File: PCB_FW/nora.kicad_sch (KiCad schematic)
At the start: 274 parts, among them J1 USB_C_Receptacle_USB2.0, J2 Conn_01x04, J3 Conn_01x02, J4 Conn_01x02, J5 Conn_02x03_Odd_Even, U1 ATmega32U4-MU, U2 24LC64, U4 Pico, Y1 16MHz

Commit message: WIP 配線中
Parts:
- RE_42: footprint locallib:RotaryEncoder_Alps_EC11K-Switch_Vertical_H20mm -> Rotary_Encoder:RotaryEncoder_Alps_EC11E-Switch_Vertical_H20mm
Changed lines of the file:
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@@
     (property "Reference" "RE_42" (id 0) (at 105.41 266.5435 0))
     (property "Value" "RotaryEncoder_Switch" (id 1) (at 105.41 269.3186 0))
-    (property "Footprint" "locallib:RotaryEncoder_Alps_EC11K-Switch_Vertical_H20mm" (id 2) (at 101.6 271.526 0)
+    (property "Footprint" "Rotary_Encoder:RotaryEncoder_Alps_EC11E-Switch_Vertical_H20mm" (id 2) (at 101.6 271.526 0)
       (effects (font (size 1.27 1.27)) hide)
     )
@@
     )
     (path "/c31541b0-05b3-4f9a-a5ca-240448e17a33"
-      (reference "RE_42") (unit 1) (value "RotaryEncoder_Switch") (footprint "locallib:RotaryEncoder_Alps_EC11K-Switch_Vertical_H20mm")
+      (reference "RE_42") (unit 1) (value "RotaryEncoder_Switch") (footprint "Rotary_Encoder:RotaryEncoder_Alps_EC11E-Switch_Vertical_H20mm")
     )
     (path "/00000000-0000-0000-0000-00005b323aa5"

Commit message: ソケットのシルクに塗りを追加
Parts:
- SW_35, SW_38, SW_40, SW_41, SW_42, SW_43: footprint Keebio-Parts:Kailh-PG1350-1u-MBK-WithKeyName-Socket-1.8mm-hole-reflection -> Keebio-Parts:Kailh-PG1350-1u-MBK-WithKeyName-Socket-1.8mm-hole-reflection-frame-only
- SW_44: footprint Keebio-Parts:Kailh-PG1350-1.5u-MBK-WithKeyName-Socket-1.8mm-hole-reflection -> Keebio-Parts:Kailh-PG1350-1.5u-MBK-WithKeyName-Socket-1.8mm-hole-reflection-frame-only
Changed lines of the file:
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@@
     (property "Reference" "SW_43" (id 0) (at 161.925 95.631 0))
     (property "Value" "R4R" (id 1) (at 161.925 97.9424 0))
-    (property "Footprint" "Keebio-Parts:Kailh-PG1350-1u-MBK-WithKeyName-Socket-1.8mm-hole-reflection" (id 2) (at 161.925 97.79 0)
+    (property "Footprint" "Keebio-Parts:Kailh-PG1350-1u-MBK-WithKeyName-Socket-1.8mm-hole-reflection-frame-only" (id 2) (at 161.925 97.79 0)
       (effects (font (size 1.27 1.27)) hide)
     )
@@
     (property "Reference" "SW_40" (id 0) (at 161.925 30.861 0))
     (property "Value" "R1R" (id 1) (at 161.925 33.1724 0))
-    (property "Footprint" "Keebio-Parts:Kailh-PG1350-1u-MBK-WithKeyName-Socket-1.8mm-hole-reflection" (id 2) (at 161.925 33.02 0)
+    (property "Footprint" "Keebio-Parts:Kailh-PG1350-1u-MBK-WithKeyName-Socket-1.8mm-hole-reflection-frame-only" (id 2) (at 161.925 33.02 0)
       (effects (font (size 1.27 1.27)) hide)
     )
@@
     (property "Reference" "SW_42" (id 0) (at 161.925 74.041 0))
     (property "Value" "R3C" (id 1) (at 161.925 76.3524 0))
-    (property "Footprint" "Keebio-Parts:Kailh-PG1350-1u-MBK-WithKeyName-Socket-1.8mm-hole-reflection" (id 2) (at 161.925 76.2 0)
+    (property "Footprint" "Keebio-Parts:Kailh-PG1350-1u-MBK-WithKeyName-Socket-1.8mm-hole-reflection-frame-only" (id 2) (at 161.925 76.2 0)
       (effects (font (size 1.27 1.27)) hide)
     )
@@
     (property "Reference" "SW_44" (id 0) (at 161.925 114.681 0))
     (property "Value" "Center 1.5u" (id 1) (at 161.925 116.9924 0))
-    (property "Footprint" "Keebio-Parts:Kailh-PG1350-1.5u-MBK-WithKeyName-Socket-1.8mm-hole-reflection" (id 2) (at 161.925 116.84 0)
+    (property "Footprint" "Keebio-Parts:Kailh-PG1350-1.5u-MBK-WithKeyName-Socket-1.8mm-hole-reflection-frame-only" (id 2) (at 161.925 116.84 0)
       (effects (font (size 1.27 1.27)) hide)
     )
@@
     (property "Reference" "SW_38" (id 0) (at 145.415 95.631 0))
     (property "Value" "R4L" (id 1) (at 145.415 97.9424 0))
-    (property "Footprint" "Keebio-Parts:Kailh-PG1350-1u-MBK-WithKeyName-Socket-1.8mm-hole-reflection" (id 2) (at 145.415 97.79 0)
+    (property "Footprint" "Keebio-Parts:Kailh-PG1350-1u-MBK-WithKeyName-Socket-1.8mm-hole-reflection-frame-only" (id 2) (at 145.415 97.79 0)
       (effects (font (size 1.27 1.27)) hide)
     )
@@
     (property "Reference" "SW_41" (id 0) (at 161.925 52.451 0))
     (property "Value" "R2C" (id 1) (at 161.925 54.7624 0))
-    (property "Footprint" "Keebio-Parts:Kailh-PG1350-1u-MBK-WithKeyName-Socket-1.8mm-hole-reflection" (id 2) (at 161.925 54.61 0)
+    (property "Footprint" "Keebio-Parts:Kailh-PG1350-1u-MBK-WithKeyName-Socket-1.8mm-hole-reflection-frame-only" (id 2) (at 161.925 54.61 0)
       (effects (font (size 1.27 1.27)) hide)
     )
@@
     (property "Reference" "SW_35" (id 0) (at 145.415 30.861 0))
     (property "Value" "R1L" (id 1) (at 145.415 33.1724 0))
-    (property "Footprint" "Keebio-Parts:Kailh-PG1350-1u-MBK-WithKeyName-Socket-1.8mm-hole-reflection" (id 2) (at 145.415 33.02 0)
+    (property "Footprint" "Keebio-Parts:Kailh-PG1350-1u-MBK-WithKeyName-Socket-1.8mm-hole-reflection-frame-only" (id 2) (at 145.415 33.02 0)
       (effects (font (size 1.27 1.27)) hide)
     )
@@
     )
     (path "/efce3ccf-dccf-4ab2-825c-383d2306383e"
-      (reference "SW_35") (unit 1) (value "R1L") (footprint "Keebio-Parts:Kailh-PG1350-1u-MBK-WithKeyName-Socket-1.8mm-hole-reflection")
+      (reference "SW_35") (unit 1) (value "R1L") (footprint "Keebio-Parts:Kailh-PG1350-1u-MBK-WithKeyName-Socket-1.8mm-hole-reflection-frame-only")
     )
     (path "/00000000-0000-0000-0000-000061ce9654"
@@
     )
     (path "/cc1d72d3-c085-42d5-b51a-f25583124fcb"
-      (reference "SW_38") (unit 1) (value "R4L") (footprint "Keebio-Parts:Kailh-PG1350-1u-MBK-WithKeyName-Socket-1.8mm-hole-reflection")
+      (reference "SW_38") (unit 1) (value "R4L") (footprint "Keebio-Parts:Kailh-PG1350-1u-MBK-WithKeyName-Socket-1.8mm-hole-reflection-frame-only")
     )
     (path "/00000000-0000-0000-0000-000061ce969c"
@@
     )
     (path "/164abd3f-e22c-4c79-a335-ba856dad611c"
-      (reference "SW_40") (unit 1) (value "R1R") (footprint "Keebio-Parts:Kailh-PG1350-1u-MBK-WithKeyName-Socket-1.8mm-hole-reflection")
+      (reference "SW_40") (unit 1) (value "R1R") (footprint "Keebio-Parts:Kailh-PG1350-1u-MBK-WithKeyName-Socket-1.8mm-hole-reflection-frame-only")
     )
     (path "/ef3363f5-8d79-4ecf-984c-7cb0bf9cde9e"
-      (reference "SW_41") (unit 1) (value "R2C") (footprint "Keebio-Parts:Kailh-PG1350-1u-MBK-WithKeyName-Socket-1.8mm-hole-reflection")
+      (reference "SW_41") (unit 1) (value "R2C") (footprint "Keebio-Parts:Kailh-PG1350-1u-MBK-WithKeyName-Socket-1.8mm-hole-reflection-frame-only")
     )
     (path "/8f0205a6-0769-462f-bc35-3f1d10f4a746"
-      (reference "SW_42") (unit 1) (value "R3C") (footprint "Keebio-Parts:Kailh-PG1350-1u-MBK-WithKeyName-Socket-1.8mm-hole-reflection")
+      (reference "SW_42") (unit 1) (value "R3C") (footprint "Keebio-Parts:Kailh-PG1350-1u-MBK-WithKeyName-Socket-1.8mm-hole-reflection-frame-only")
     )
     (path "/0dea41fa-0c6a-48a7-81ed-660971009e1c"
-      (reference "SW_43") (unit 1) (value "R4R") (footprint "Keebio-Parts:Kailh-PG1350-1u-MBK-WithKeyName-Socket-1.8mm-hole-reflection")
+      (reference "SW_43") (unit 1) (value "R4R") (footprint "Keebio-Parts:Kailh-PG1350-1u-MBK-WithKeyName-Socket-1.8mm-hole-reflection-frame-only")
     )
     (path "/a2f8a0fb-e12c-4d2c-8033-a042712e74d5"
-      (reference "SW_44") (unit 1) (value "Center 1.5u") (footprint "Keebio-Parts:Kailh-PG1350-1.5u-MBK-WithKeyName-Socket-1.8mm-hole-reflection")
+      (reference "SW_44") (unit 1) (value "Center 1.5u") (footprint "Keebio-Parts:Kailh-PG1350-1.5u-MBK-WithKeyName-Socket-1.8mm-hole-reflection-frame-only")
     )
     (path "/00000000-0000-0000-0000-000061d01246"

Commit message: 基板製造ファイル準備
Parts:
- D99: LCSC (none) -> C81598
- R7: LCSC (none) -> C17513
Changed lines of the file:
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@@
+      (effects (font (size 1.27 1.27)) hide)
+    )
+    (property "LCSC" "C81598" (id 4) (at 290.195 179.07 0)
       (effects (font (size 1.27 1.27)) hide)
     )
@@
       (effects (font (size 1.27 1.27)) hide)
     )
+    (property "LCSC" "C17513" (id 4) (at 297.815 176.53 0)
+      (effects (font (size 1.27 1.27)) hide)
+    )

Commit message: パーツ番号変更
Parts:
- C1: LCSC C15850 -> C2922480
- U2: Alternative LCSC (none) -> C6487, C116707, C13645
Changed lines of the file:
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@@
       (effects (font (size 1.27 1.27)) hide)
     )
-    (property "LCSC" "C15850" (id 4) (at 329.565 120.015 0)
+    (property "LCSC" "C2922480" (id 4) (at 329.565 120.015 0)
       (effects (font (size 1.27 1.27)) hide)
     )
@@
       (effects (font (size 1.27 1.27)) hide)
     )
+    (property "Alternative LCSC" "C6487, C116707, C13645" (id 5) (at 386.715 168.91 0)
+      (effects (font (size 1.27 1.27)) hide)
+    )

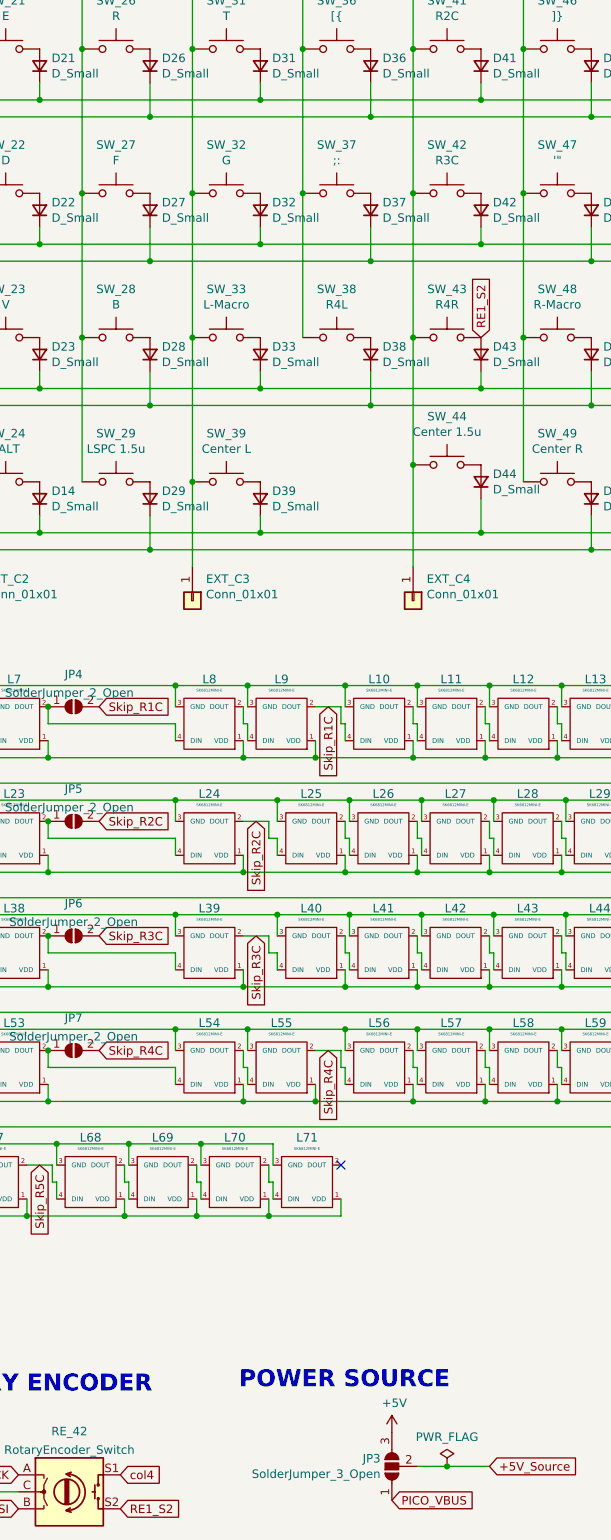
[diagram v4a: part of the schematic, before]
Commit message: ロータリーエンコーダが接続されるマトリクス行を変更
物理的にREが配置される場所に合わせた行へ修正。
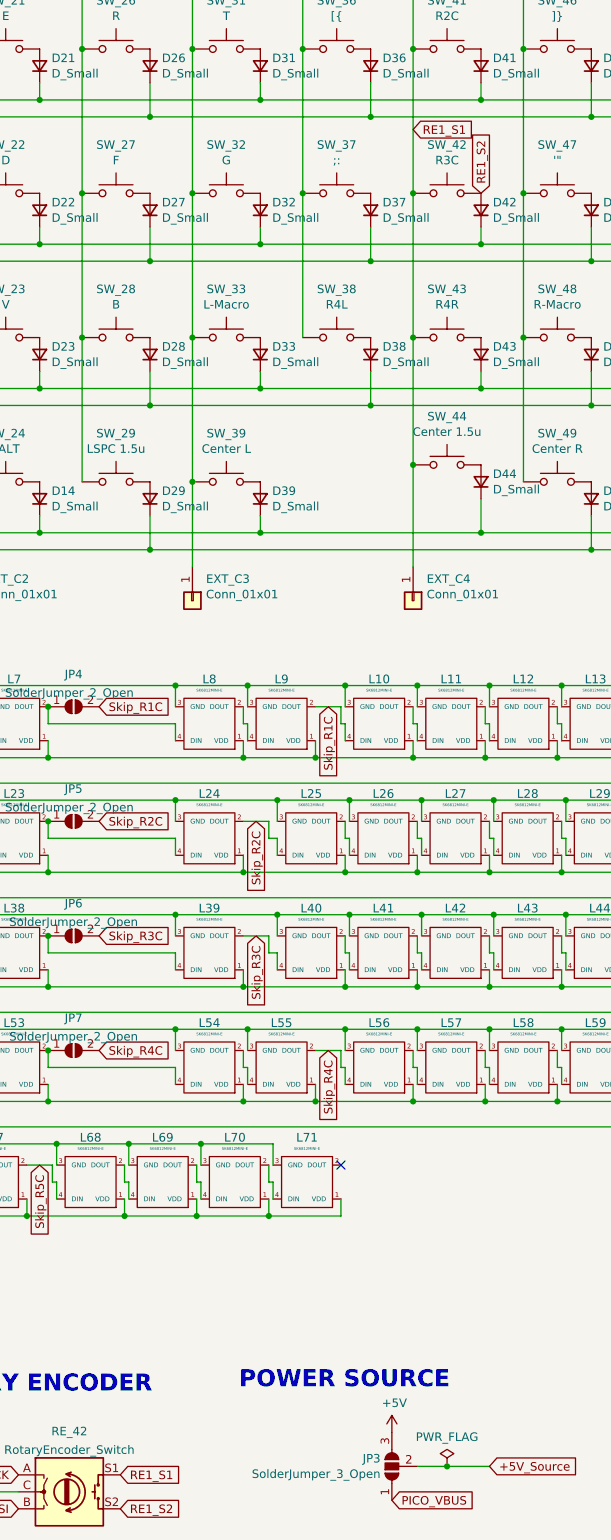
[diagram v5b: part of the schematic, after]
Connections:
- net RE1_S2: now also D42.2 (A), SW_42.2; no longer D43.2 (A), SW_43.2
- net col4 renamed RE1_S1
- new net: D43.2 (A), SW_43.2
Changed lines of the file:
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@@
     )
   )
-  (global_label "col4" (shape input) (at 113.03 273.05 0) (fields_autoplaced)
-    (effects (font (size 1.27 1.27)) (justify left))
-    (property "シート間のリファレンス" "${INTERSHEET_REFS}" (id 0) (at 119.4666 272.9706 0)
+  (global_label "RE1_S1" (shape input) (at 113.03 273.05 0) (fields_autoplaced)
+    (effects (font (size 1.27 1.27)) (justify left))
+    (property "シート間のリファレンス" "${INTERSHEET_REFS}" (id 0) (at 122.3694 272.9706 0)
       (effects (font (size 1.27 1.27)) (justify left) hide)
     )
@@
     )
   )
+  (global_label "RE1_S1" (shape input) (at 156.845 71.755 0) (fields_autoplaced)
+    (effects (font (size 1.27 1.27)) (justify left))
+    (property "シート間のリファレンス" "${INTERSHEET_REFS}" (id 0) (at 166.1844 71.6756 0)
+      (effects (font (size 1.27 1.27)) (justify left) hide)
+    )
+  )
   (global_label "row0" (shape input) (at 389.255 85.725 0) (fields_autoplaced)
     (effects (font (size 1.27 1.27)) (justify left))
@@
     )
   )
-  (global_label "RE1_S2" (shape input) (at 167.005 102.87 90) (fields_autoplaced)
-    (effects (font (size 1.27 1.27)) (justify left))
-    (property "シート間のリファレンス" "${INTERSHEET_REFS}" (id 0) (at 166.9256 93.5306 90)
-      (effects (font (size 1.27 1.27)) (justify left) hide)
-    )
+  (global_label "RE1_S2" (shape input) (at 167.005 81.28 90) (fields_autoplaced)
+    (effects (font (size 1.27 1.27)) (justify left))
+    (property "シート間のリファレンス" "${INTERSHEET_REFS}" (id 0) (at 166.9256 71.9406 90)
+      (effects (font (size 1.27 1.27)) (justify left) hide)
+    )

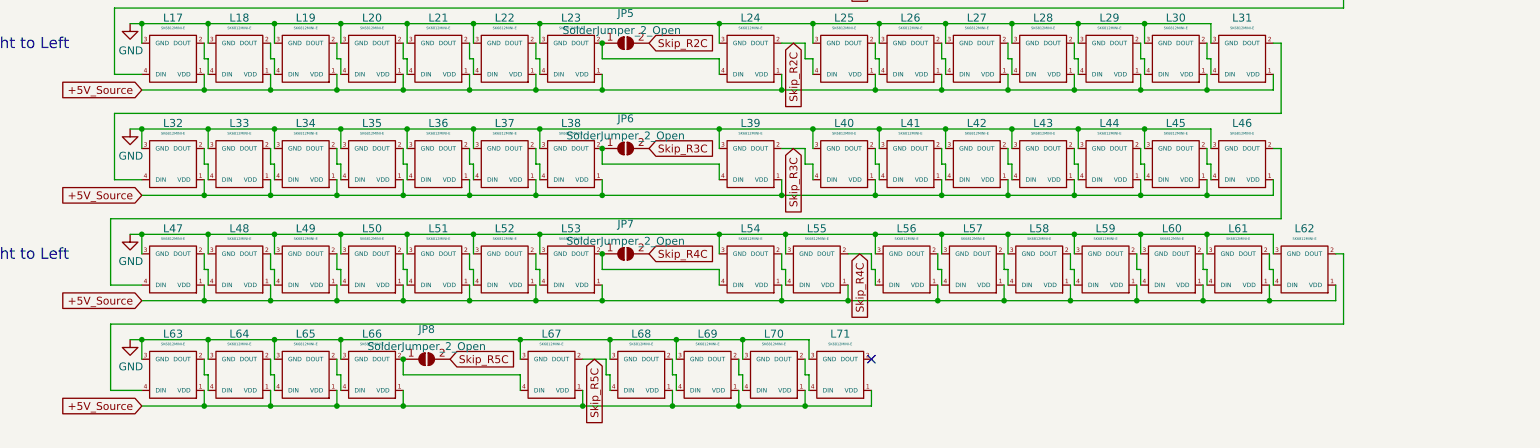
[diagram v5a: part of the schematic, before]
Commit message: FW-PCB: Add jumper to skip LEDs with FW+RE layout #85
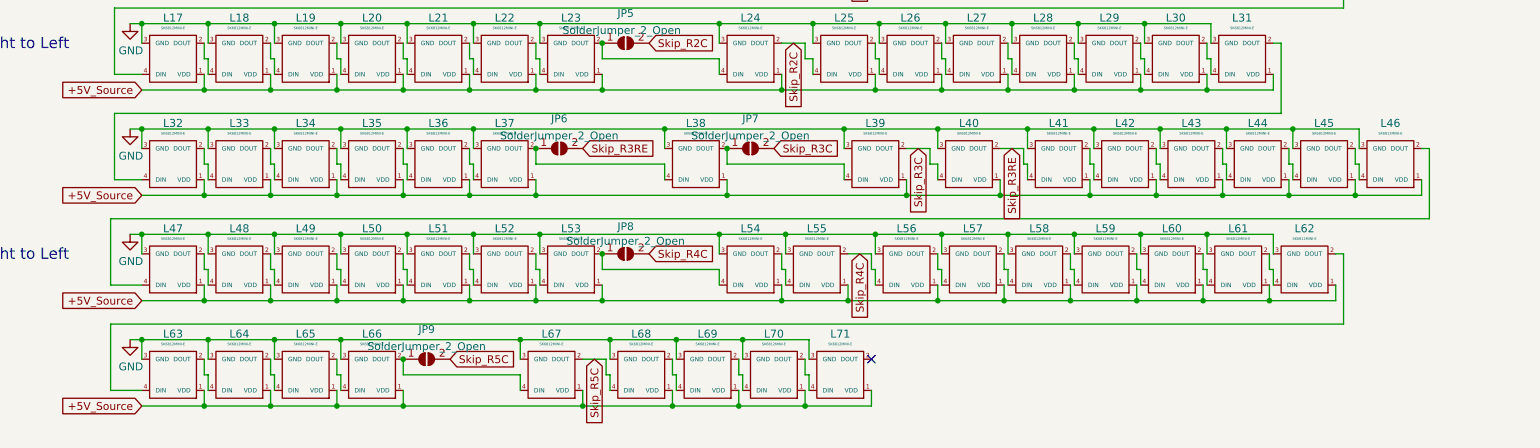
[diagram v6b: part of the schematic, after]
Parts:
- added JP6: SolderJumper_2_Open, Jumper:SolderJumper-2_P1.3mm_Open_RoundedPad1.0x1.5mm, symbol Jumper:SolderJumper_2_Open
- renumbered JP6 to JP7, JP7 to JP8, JP8 to JP9
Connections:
- net at L37.2 (DOUT), L38.4 (DIN): now also JP6.1 (A)
- net Skip_R3RE: now reaches L40.2 (DOUT), L41.4 (DIN)
- net Skip_R3RE: now also JP6.2 (B)
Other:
- moved on the sheet: JP7, L38, L39, L40, L41, L42, L43, L44, L45, L46
